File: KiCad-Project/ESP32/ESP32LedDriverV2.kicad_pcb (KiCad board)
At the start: 4 copper layers, 100 x 57 mm, 55 parts, among them J1 Power, J2 LED Terminal, J3 UART, Q1 PMOS 30V, Q10 Q_NMOS_GDS, Q2 S8050, Q3 Q_NMOS_GDS, Q4 Q_NMOS_GDS, Q5 Q_NMOS_GDS, Q6 Q_NMOS_GDS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

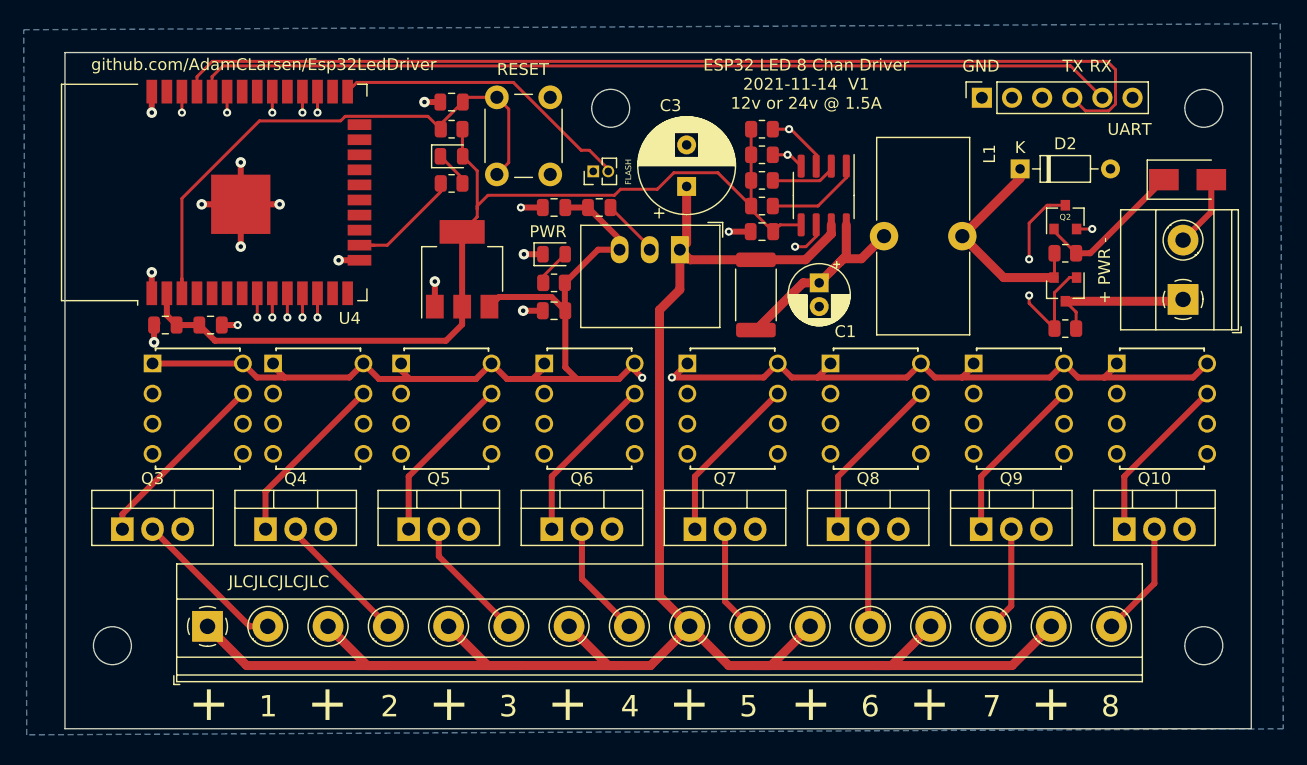
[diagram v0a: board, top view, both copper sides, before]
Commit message: Refine PCB layout
Added GPIO labels to the bottom of the board
updates to ESP32 power and ground traces
Removed zip file of plot files.
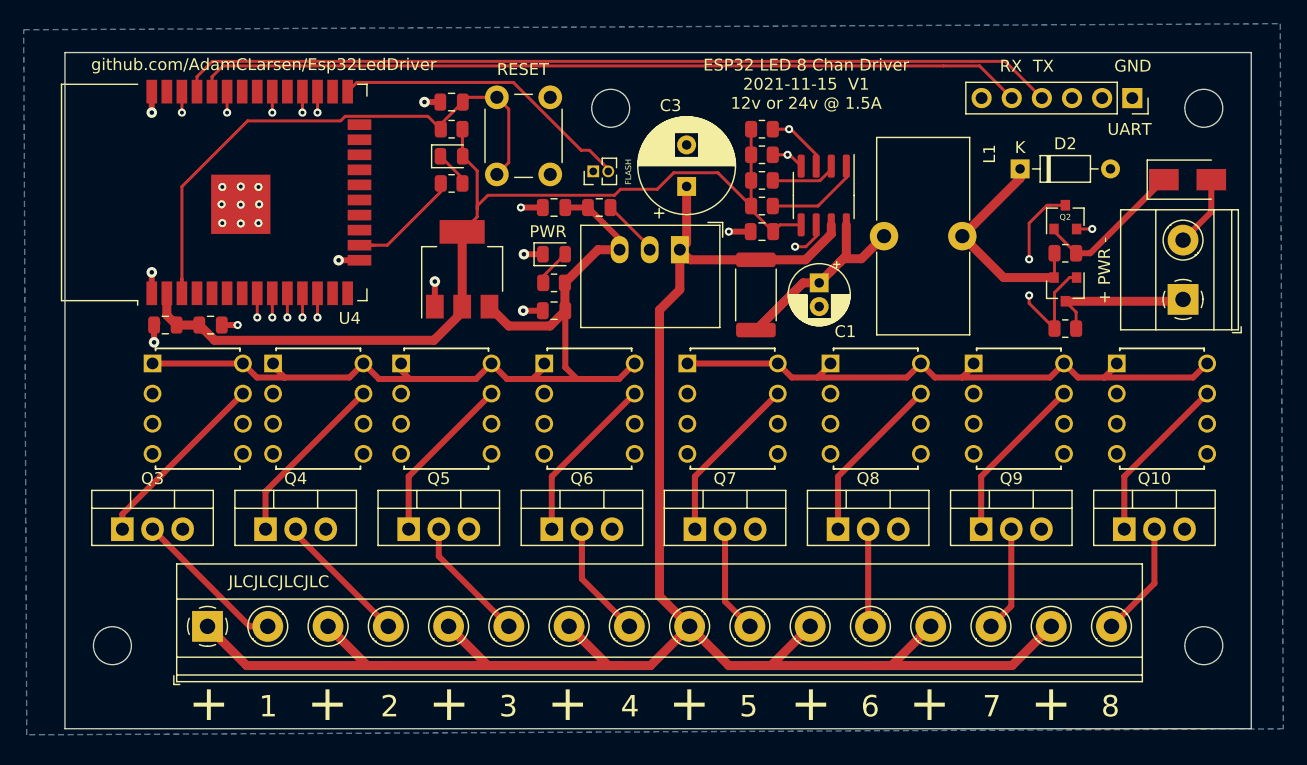
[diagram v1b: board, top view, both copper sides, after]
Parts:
- moved J3 12.7 mm to (134.0, 65.8), turned to 270 degrees
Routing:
- net /ESP32/UART_TX: track 86.7 -> 74.3 mm
- net /ESP32/UART_RX: track 77.8 -> 70.2 mm
- net +5V: track 136.0 -> 133.8 mm, vias 2 -> 0
- net GND: track 52.7 -> 54.7 mm, vias 17 -> 22
- net +3V3: track 83.7 -> 83.1 mm
- net /ESP32/~RESET: track 47.8 -> 48.4 mm
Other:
- board text added: "CHAN 1 - IO32 CHAN 2 - IO33 CHAN 3 - IO25 CHAN 4 - IO26 CHAN 5 - IO27 CHAN 6 - IO18 CHAN 7 - IO17 CHAN 8 - IO16"
- board text added: "ESP32 LED 8 Chan Driver 2021-11-15 V1 12v or 24v @ 1.5A"
- board text added: "ESP32 Pin layout: LED - IO13 SDA - IO21 SCL - IO22"
- board text removed: "ESP32 LED 8 Chan Driver 2021-11-14 V1 12v or 24v @ 1.5A"

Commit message: Increased trace width for +24v net
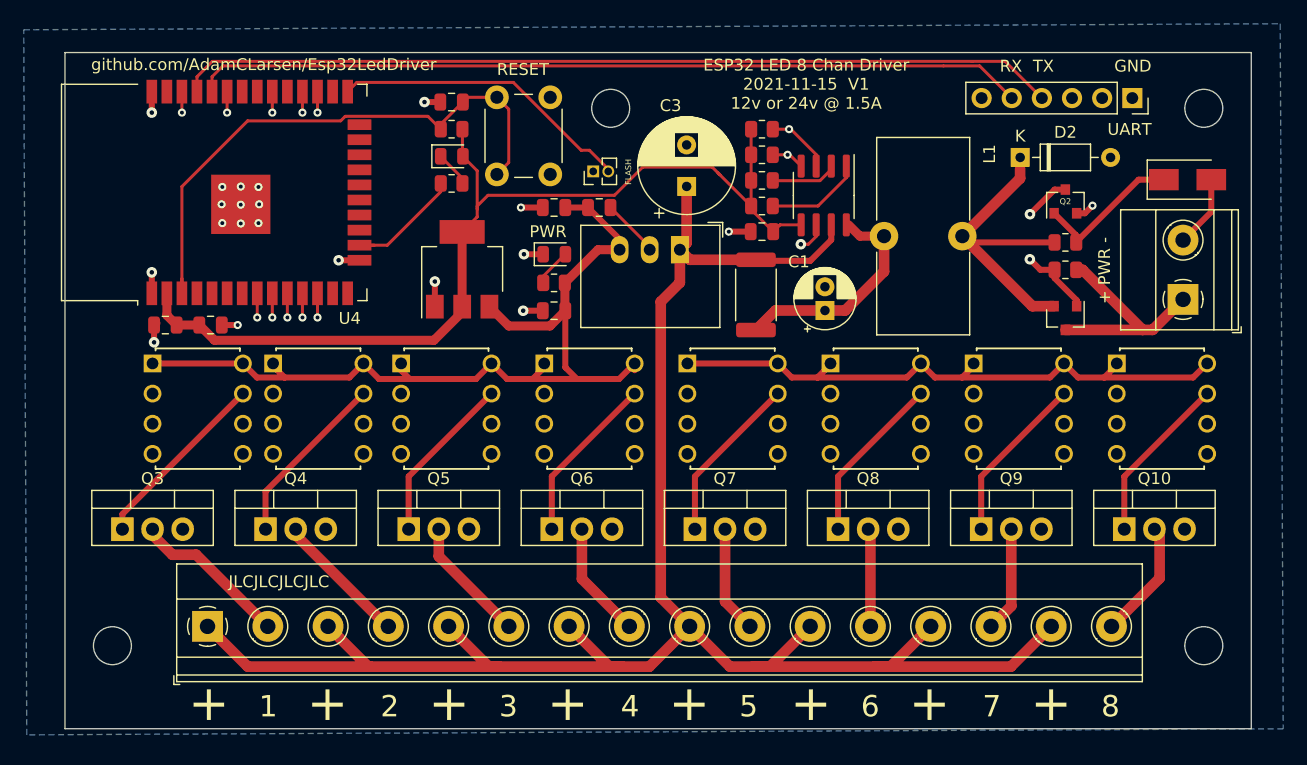
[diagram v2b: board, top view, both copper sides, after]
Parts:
- moved R1 4.95 mm to (128.3, 80.3)
- moved Q1 2.41 mm to (128.3, 84.4)
- moved C1 2.38 mm to (108.1, 83.7), turned to 90 degrees
- moved Q2 1.32 mm to (128.3, 74.6)
- moved D2 0.97 mm to (124.5, 70.8)
- moved R2 0.91 mm to (128.3, 78.0)
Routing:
- net +24V_SW: track 19.8 -> 26.7 mm
- net /+24V_RAW: track 12.7 -> 18.9 mm
- net Net-(Q1-Pad1): track 18.9 -> 13.9 mm
- net +24V: track 162.4 -> 159.9 mm
- net +24V_IN: track 18.3 -> 19.2 mm
- net +3V3: track 83.1 -> 83.7 mm
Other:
- net class +24v: clearance 0.227 -> 0.7; trace_width 0.762 -> 0.9

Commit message: Removed reverse voltage and increased size of power traces
Reverse voltage needed different components for 24 volt, and was a nice to have, so to keep cost down, opted to remove it.
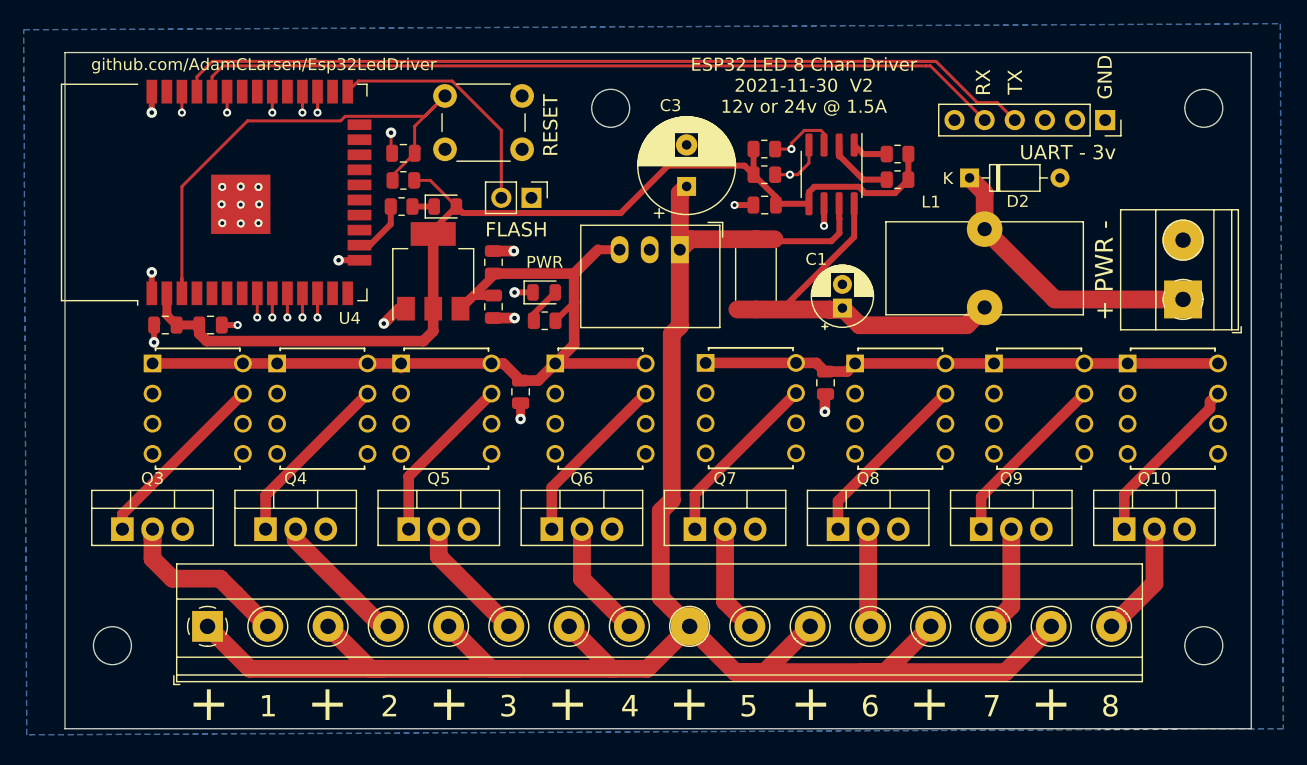
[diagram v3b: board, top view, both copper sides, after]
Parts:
- removed D1: D, Diode_SMD:D_SMA
- removed Q1: PMOS 30V, Package_TO_SOT_SMD:SOT-23
- removed Q2: S8050, Package_TO_SOT_SMD:SOT-23
- removed R1, R2: 10K, Resistor_SMD:R_0805_2012Metric
- added C10: 22uF, Capacitor_SMD:C_0805_2012Metric, F.Cu at (108.1, 89.8)
- JP1: footprint Connector_PinHeader_1.27mm:PinHeader_1x02_P1.27mm_Vertical -> Connector_PinHeader_2.54mm:PinHeader_1x02_P2.54mm_Vertical
- moved R6 12.2 mm to (114.2, 70.6), turned to 180 degrees
- moved R7 11.4 mm to (114.2, 72.7), turned to 180 degrees
- moved C5 10.0 mm to (80.1, 79.7), turned to 90 degrees
- moved C4 9.80 mm to (80.1, 83.4), turned to 270 degrees
- moved C7 7.40 mm to (82.4, 90.6), turned to 270 degrees
- moved C6 5.93 mm to (72.5, 70.5)
- moved R9 5.93 mm to (72.5, 72.8)
- moved JP1 5.66 mm to (83.3, 74.2), turned to 270 degrees
- moved SW1 4.98 mm to (82.5, 70.2), turned to 180 degrees
- moved R10 4.64 mm to (72.4, 75.0)
- moved D2 4.60 mm to (120.3, 72.6)
- moved LED2 4.27 mm to (76.1, 75.0)
- moved LED1 3.33 mm to (84.4, 82.2)
- moved R8 3.29 mm to (84.4, 84.6)
- moved J3 2.94 mm to (131.7, 67.7)
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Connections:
- J1 pad 1: /+24V_RAW -> +24V_SW
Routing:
- net /+24V_RAW: track 18.9 -> 0.00 mm
- net +24V_IN: track 19.2 -> 36.4 mm
- net Net-(Q1-Pad1): track 13.9 -> 0.00 mm, vias 2 -> 0
- net Net-(D1-Pad1): track 12.8 -> 0.00 mm
- net +5V: track 133.8 -> 122.8 mm
- net GND: track 54.5 -> 44.6 mm, vias 22 -> 23
- net +24V: track 159.9 -> 168.5 mm
- net +3V3: track 83.7 -> 90.1 mm
- net Net-(R10-Pad1): track 10.7 -> 4.86 mm
- net Net-(R6-Pad2): track 8.16 -> 3.06 mm
- net /ESP32/~FLASH: track 25.5 -> 20.7 mm
- net /ESP32/~RESET: track 48.4 -> 44.0 mm
- net /Z5: track 36.8 -> 41.0 mm
- net SCL: track 62.5 -> 66.0 mm
- net /Z6: track 66.1 -> 68.7 mm
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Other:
- net class +24v: clearance 0.7 -> 0.6
- board text added: "ESP32 LED 8 Chan Driver 2021-11-30 V2 12v or 24v @ 1.5A"
- board text added: "UART - 3v"
- board text removed: "ESP32 LED 8 Chan Driver 2021-11-15 V1 12v or 24v @ 1.5A"
- board text removed: "JLCJLCJLCJLC"
- board text removed: "UART"

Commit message: Jumper to connect UART VCC to 5v
Allow powering the 3v-5v side from the UART conector.
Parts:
- added JP2: UART_VCC, Connector_PinHeader_2.54mm:PinHeader_1x02_P2.54mm_Vertical, F.Cu at (87.3, 74.2)
- C5: value 10pF -> 22uF
- R8: value 1K -> 2.2K
- turned LED2 to 180 degrees
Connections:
- J3 pad 3: (no net) -> /ESP32/UART_VCC
- LED2 pad 1: Net-(LED2-Pad1) -> GND
- LED2 pad 2: +3V3 -> Net-(LED2-Pad2)
- R10 pad 2: Net-(LED2-Pad1) -> Net-(LED2-Pad2)
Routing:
- net +24V: track 168.5 -> 9.88 mm
- net /ESP32/UART_VCC: track 0.00 -> 40.2 mm, vias 0 -> 1
- net +5V: track 122.8 -> 127.8 mm
- net +3V3: track 90.1 -> 92.5 mm
- net Net-(LED2-Pad2): track 0.00 -> 1.83 mm
- net Net-(LED2-Pad1): track 1.83 -> 0.00 mm
- net /Z1-: track 15.5 -> 17.0 mm
- net GND: track 44.6 -> 46.0 mm, vias 23 -> 24
- net /Z2-: track 11.7 -> 13.1 mm
- added copper zone on F.Cu, net +24V
- added copper zone on F.Cu, net +24V_IN
- added copper zone on F.Cu, net +24V_SW
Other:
- board text added: "ESP32 LED 8 Chan Driver 2021-11-30 V2 12v to 24v @ 1.5A"
- board text added: "VCC"
- board text removed: "ESP32 LED 8 Chan Driver 2021-11-30 V2 12v or 24v @ 1.5A"

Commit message: Update fill zones
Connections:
- JP2 pad 1: +5V -> +3V3
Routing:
- net +24V_IN: track 36.4 -> 12.2 mm
- net +24V_SW: track 24.2 -> 0.22 mm
- net +5V: track 127.8 -> 122.8 mm
- net Net-(Q10-Pad1): track 14.7 -> 16.2 mm
- net Net-(Q3-Pad1): track 15.6 -> 16.9 mm
- net /Z3: track 16.2 -> 15.2 mm
- net +3V3: track 92.5 -> 91.9 mm
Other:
- board text added: "+3v"
- board text removed: "VCC"

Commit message: Move on board test LED to a better pin. and swap TX/RX UART pins
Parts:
- moved JP1 2.57 mm to (80.8, 74.3), turned to 90 degrees
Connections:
- J3 pad 4: /ESP32/UART_TX -> /ESP32/UART_RX
- J3 pad 5: /ESP32/UART_RX -> /ESP32/UART_TX
- U4 pad 16: Net-(R10-Pad1) -> (no net)
- U4 pad 31: (no net) -> Net-(R10-Pad1)
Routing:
- net Net-(R10-Pad1): track 4.86 -> 20.0 mm
- net /ESP32/~FLASH: track 20.7 -> 21.8 mm
- net /ESP32/~RESET: track 44.0 -> 44.3 mm, vias 0 -> 1
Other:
- board text added: "ESP32 Pin layout: LED - IO19 SDA - IO21 SCL - IO22"
- board text removed: "ESP32 Pin layout: LED - IO13 SDA - IO21 SCL - IO22"

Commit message: Aligning parts to each other
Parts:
- added JP10: Driver Bypass, Jumper:SolderJumper-2_P1.3mm_Open_RoundedPad1.0x1.5mm, F.Cu at (137.5, 90.7)
- added JP3: Driver Bypass, Jumper:SolderJumper-2_P1.3mm_Open_RoundedPad1.0x1.5mm, F.Cu at (55.2, 90.8)
- added JP4: Driver Bypass, Jumper:SolderJumper-2_P1.3mm_Open_RoundedPad1.0x1.5mm, F.Cu at (65.6, 90.7)
- added JP5: Driver Bypass, Jumper:SolderJumper-2_P1.3mm_Open_RoundedPad1.0x1.5mm, F.Cu at (76.2, 90.7)
- added JP6: Driver Bypass, Jumper:SolderJumper-2_P1.3mm_Open_RoundedPad1.0x1.5mm, F.Cu at (89.3, 90.7)
- added JP7: Driver Bypass, Jumper:SolderJumper-2_P1.3mm_Open_RoundedPad1.0x1.5mm, F.Cu at (102.1, 90.7)
- added JP8: Driver Bypass, Jumper:SolderJumper-2_P1.3mm_Open_RoundedPad1.0x1.5mm, F.Cu at (114.5, 90.7)
- added JP9: Driver Bypass, Jumper:SolderJumper-2_P1.3mm_Open_RoundedPad1.0x1.5mm, F.Cu at (126.1, 90.7)
- moved R10 0.10 mm to (72.5, 74.9)
- moved LED1 0.09 mm to (84.5, 82.2)
- moved R9 0.06 mm to (72.5, 72.8)
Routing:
- net /Z7: track 74.6 -> 81.0 mm
- net /Z8: track 85.4 -> 90.7 mm
- net /ESP32/UART_RX: track 68.6 -> 72.1 mm
- net Net-(JP4-Pad2): track 15.0 -> 18.3 mm
- net Net-(JP9-Pad2): track 15.0 -> 18.2 mm
- net Net-(JP5-Pad2): track 14.3 -> 17.5 mm
- net Net-(JP8-Pad2): track 15.2 -> 18.3 mm
- net /Z1: track 13.8 -> 16.8 mm
- net /Z6: track 68.7 -> 71.7 mm
- net Net-(JP6-Pad2): track 14.7 -> 17.7 mm
- net /ESP32/UART_TX: track 72.8 -> 69.9 mm
- net Net-(JP7-Pad2): track 15.0 -> 17.9 mm
- net /Z2: track 9.48 -> 12.3 mm
- net /Z4: track 26.7 -> 29.5 mm
- net /Z3: track 15.2 -> 17.6 mm
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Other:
- board text added: "ESP32 LED 8 Chan Driver 2021-11-30 V2 12v to 24v @ 2A"
- board text removed: "ESP32 LED 8 Chan Driver 2021-11-30 V2 12v to 24v @ 1.5A"

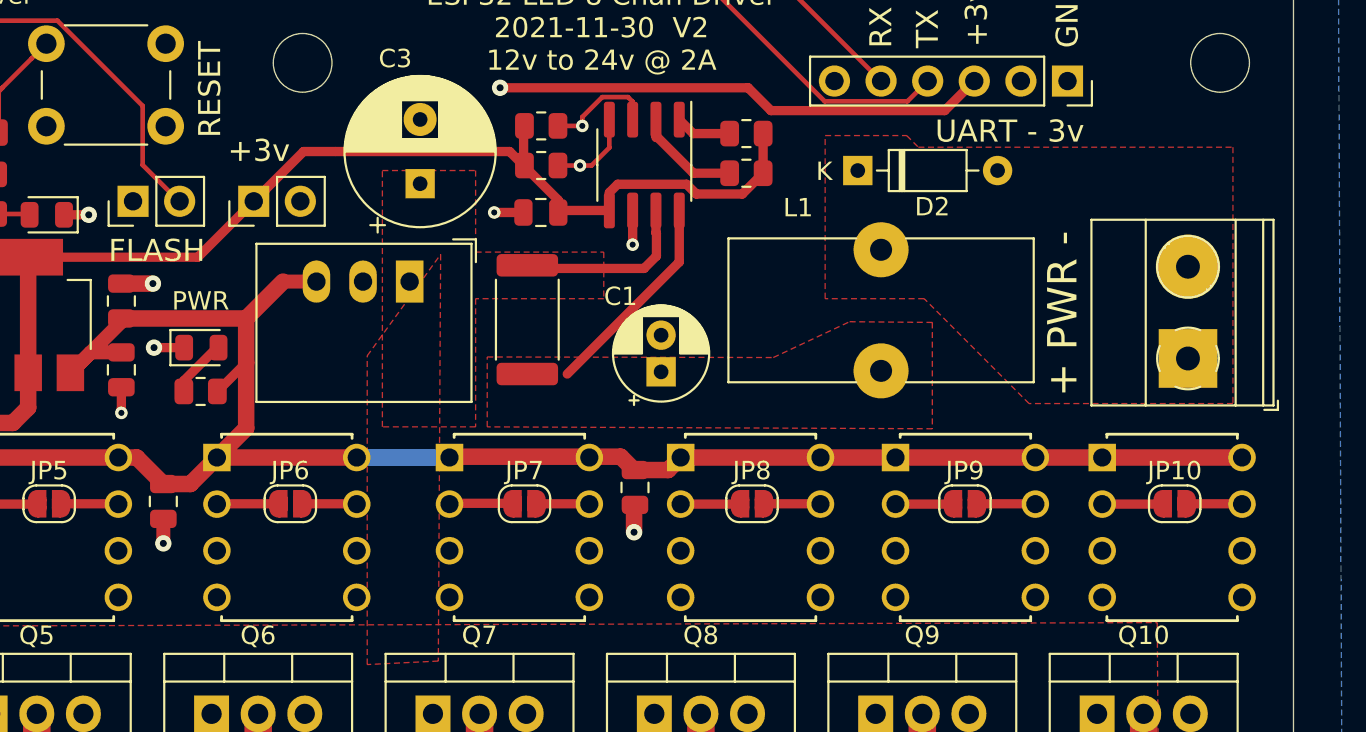
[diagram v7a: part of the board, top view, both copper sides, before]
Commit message: More clean up of PCB layout
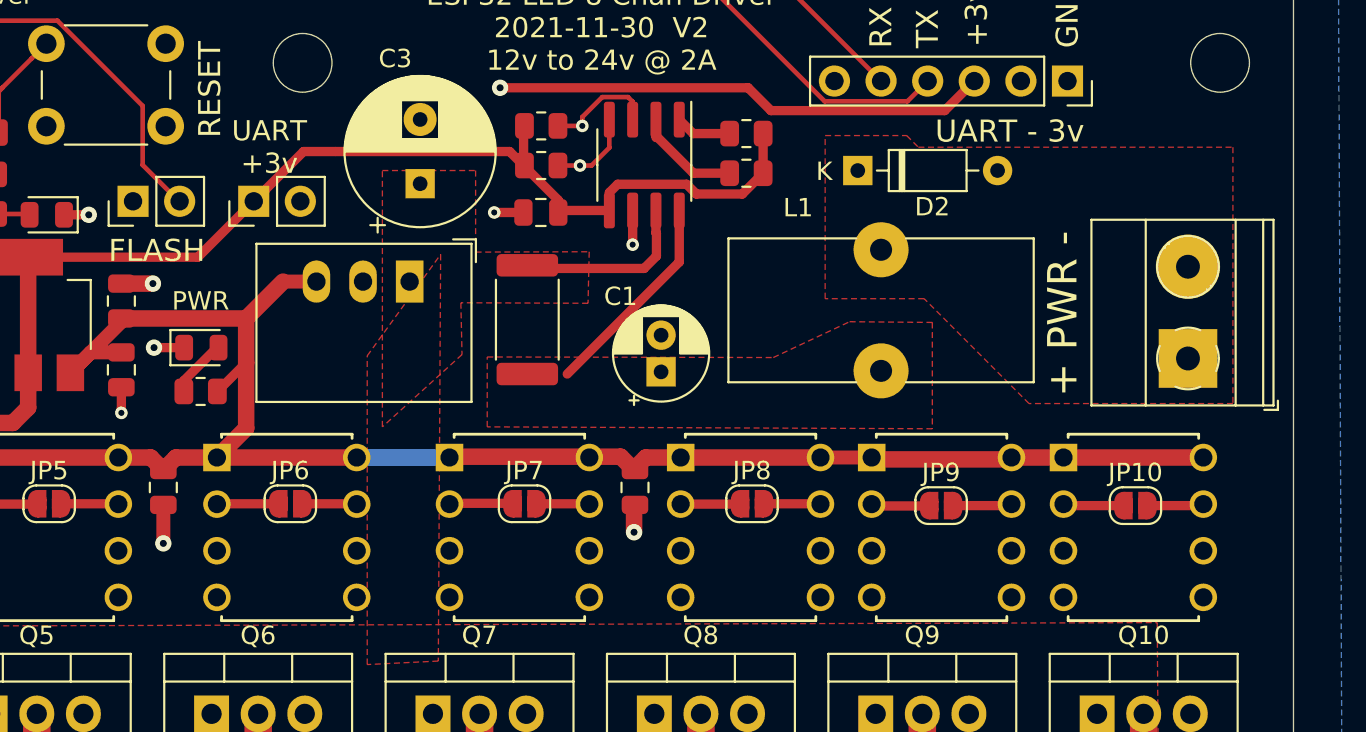
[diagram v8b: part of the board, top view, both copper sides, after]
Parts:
- moved JP10 2.14 mm to (135.4, 90.8)
- moved U12 2.11 mm to (139.1, 95.8)
- moved JP9 1.30 mm to (124.8, 90.8)
- moved U11 1.30 mm to (128.6, 95.8)
- moved C7 0.76 mm to (82.4, 89.8)
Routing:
- net +5V: track 122.8 -> 119.9 mm
- net /Z8: track 90.7 -> 88.9 mm
- net /Z7: track 81.0 -> 79.7 mm
- net Net-(JP10-Pad2): track 17.7 -> 16.9 mm
- net GND: track 45.2 -> 46.0 mm
- net Net-(JP9-Pad2): track 18.2 -> 17.7 mm
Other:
- board text added: "UART +3v"
